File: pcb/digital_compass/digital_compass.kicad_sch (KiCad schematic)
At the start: 0 parts

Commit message: Finish basic digital compass schematic.
* Based on updated xiao-based design
* Also opened in KiCad 7
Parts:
- added BT1: Battery, symbol Device:Battery
- added C1: 0.47uF, symbol Device:C
- added C2: 0.1uF, symbol Device:C
- added R1: 330, symbol Device:R
- added U1: L7805, symbol Regulator_Linear:L7805
- added U2: Seeed Studio XIAO SAMD21, symbol digital_compass:Seeed Studio XIAO SAMD21
- added U3: Level_Shifter, symbol digital_compass:Level_Shifter
- added U4: QMC5883L, symbol digital_compass:QMC5883L
- added U5: Adafruit_Neopixel_Ring_24, symbol digital_compass:Adafruit_Neopixel_Ring_24
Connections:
- new net: C2.1, U1.3 (OUT), U2.14 (5V), U3.10 (HV), U4.1 (VCC), U5.1 (PWR1), U5.2 (PWR2)
- new net: U3.12 (HV1), U4.3 (SCL)
- new net: U3.11 (HV2), U4.4 (SDA)
- new net: U2.6 (PA9_A5_D5_SCL), U3.1 (LV1)
- new net: U2.5 (PA8_A4_D4_SDA), U3.2 (LV2)
- new net: U2.12 (3V3), U3.3 (LV)
- new net: U2.7 (PB08_A6_D6_TX), U3.5 (LV3)
- new net: R1.1, U3.8 (HV3)
- new net: R1.2, U5.3 (Din)
- new net +9V: BT1.1 (+), C1.1, U1.1 (IN)
- new net GND: BT1.2 (-), C1.2, C2.2, U1.2 (GND), U2.13 (GND), U3.4 (GND), U3.9 (GND), U4.2 (GND), U5.5 (GND1), U5.6 (GND2)
- no-connect marks 0 -> 18

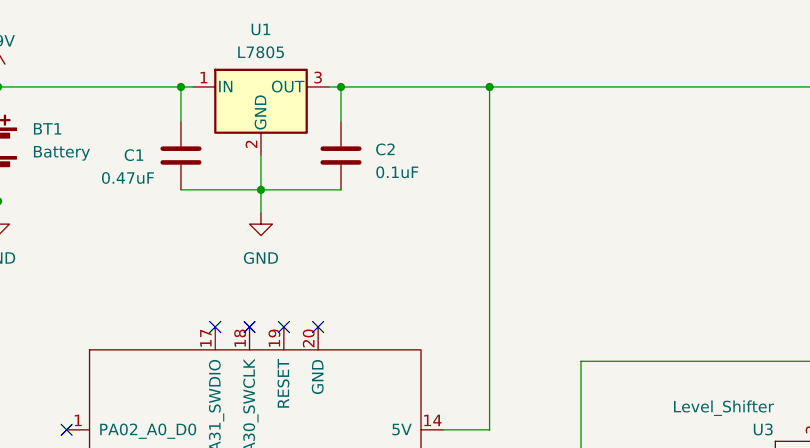
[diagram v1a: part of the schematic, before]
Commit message: Add/update footprints and run fp assignment.
The footprints for the level shifter and magnetometer boards were
created manually, but the xiao symbol/footprint were taken from
https://github.com/Seeed-Studio/OPL_Kicad_Library.

Note that the xiao symbol was lightly tweaked to pass ERC, as the pins
were not properly labeled as power inputs/outputs, bidirectional, etc.
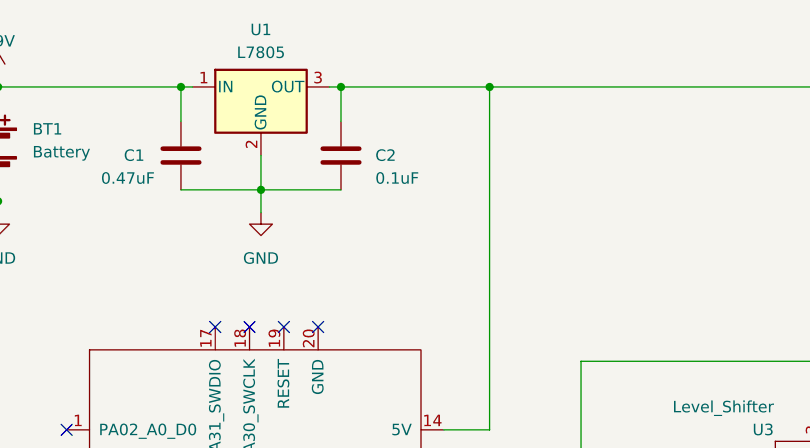
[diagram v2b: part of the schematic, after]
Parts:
- BT1: footprint (none) -> Battery:BatteryHolder_Eagle_12BH611-GR
- C1, C2: footprint (none) -> Capacitor_SMD:C_1206_3216Metric_Pad1.33x1.80mm_HandSolder
- R1: footprint (none) -> Resistor_SMD:R_1206_3216Metric_Pad1.30x1.75mm_HandSolder
- U1: footprint (none) -> Package_TO_SOT_SMD:TO-252-3_TabPin2
- U2: footprint (none) -> digital_compass:XIAO-SAMD21-RP2040-14P-2.54-21X17.8MM (Seeeduino XIAO)
- U3: footprint (none) -> digital_compass:Level_Shifter
- U4: footprint (none) -> digital_compass:QMC5883L
- U5: footprint (none) -> digital_compass:Adafruit Neopixel Ring 24
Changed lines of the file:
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@@
       (effects (font (size 1.27 1.27)) (justify left))
     )
-    (property "Footprint" "" (at 94.9452 63.5 0)
+    (property "Footprint" "Capacitor_SMD:C_1206_3216Metric_Pad1.33x1.80mm_HandSolder" (at 94.9452 63.5 0)
       (effects (font (size 1.27 1.27)) hide)
     )
@@
       (effects (font (size 1.27 1.27)))
     )
-    (property "Footprint" "" (at 103.505 55.88 0)
+    (property "Footprint" "Package_TO_SOT_SMD:TO-252-3_TabPin2" (at 103.505 55.88 0)
       (effects (font (size 1.27 1.27) italic) (justify left) hide)
     )
@@
       (effects (font (size 1.27 1.27)) (justify right))
     )
-    (property "Footprint" "" (at 205.74 97.79 0)
+    (property "Footprint" "digital_compass:QMC5883L" (at 205.74 97.79 0)
       (effects (font (size 1.27 1.27)) hide)
     )
@@
       (effects (font (size 1.27 1.27)) (justify left))
     )
-    (property "Footprint" "" (at 168.91 102.87 0)
+    (property "Footprint" "digital_compass:Level_Shifter" (at 168.91 102.87 0)
       (effects (font (size 1.27 1.27)) hide)
     )
@@
       (effects (font (size 1.27 1.27)) (justify left))
     )
-    (property "Footprint" "" (at 73.66 56.896 90)
+    (property "Footprint" "Battery:BatteryHolder_Eagle_12BH611-GR" (at 73.66 56.896 90)
       (effects (font (size 1.27 1.27)) hide)
     )
@@
       (effects (font (size 1.27 1.27)) (justify left))
     )
-    (property "Footprint" "" (at 187.452 118.11 90)
+    (property "Footprint" "Resistor_SMD:R_1206_3216Metric_Pad1.30x1.75mm_HandSolder" (at 187.452 118.11 90)
       (effects (font (size 1.27 1.27)) hide)
     )
@@
       (effects (font (size 1.27 1.27)) (justify left))
     )
-    (property "Footprint" "" (at 93.98 96.52 0)
+    (property "Footprint" "digital_compass:XIAO-SAMD21-RP2040-14P-2.54-21X17.8MM (Seeeduino XIAO)" (at 93.98 96.52 0)
       (effects (font (size 1.27 1.27)) hide)
     )
@@
   )
   (symbol (lib_id "Device:C") (at 111.76 59.69 0) (unit 1)
-    (in_bom yes) (on_board yes) (dnp no) (fields_autoplaced)
-    (property "Reference" "C2" (at 115.57 59.055 0)
-      (effects (font (size 1.27 1.27)) (justify left))
-    )
-    (property "Value" "0.1uF" (at 115.57 61.595 0)
-      (effects (font (size 1.27 1.27)) (justify left))
-    )
-    (property "Footprint" "" (at 112.7252 63.5 0)
+    (in_bom yes) (on_board yes) (dnp no)
+    (property "Reference" "C2" (at 115.57 59.69 0)
+      (effects (font (size 1.27 1.27)) (justify left))
+    )
+    (property "Value" "0.1uF" (at 115.57 62.23 0)
+      (effects (font (size 1.27 1.27)) (justify left))
+    )
+    (property "Footprint" "Capacitor_SMD:C_1206_3216Metric_Pad1.33x1.80mm_HandSolder" (at 112.7252 63.5 0)
       (effects (font (size 1.27 1.27)) hide)
     )
@@
       (effects (font (size 1.27 1.27)))
     )
-    (property "Footprint" "" (at 241.3 97.79 0)
-      (effects (font (size 1.27 1.27)) hide)
-    )
+    (property "Footprint" "digital_compass:Adafruit Neopixel Ring 24" (at 241.3 97.79 0)
+      (effects (font (size 1.27 1.27)) hide)
+    )

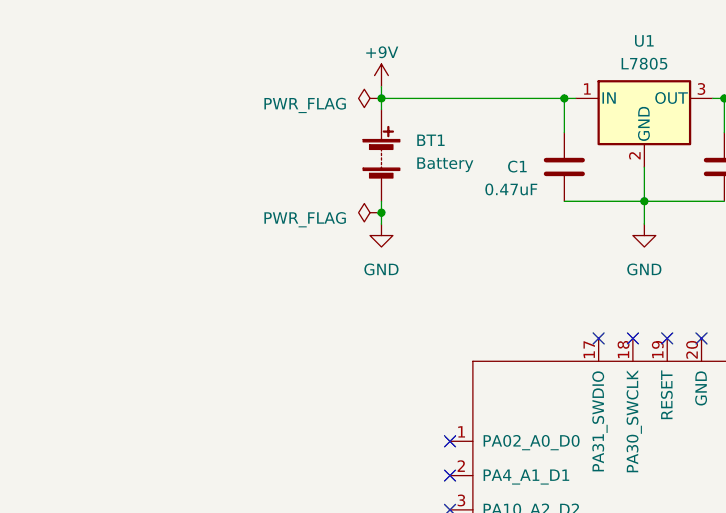
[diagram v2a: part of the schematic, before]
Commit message: Add SPDT slide power switch.
For now we just choose an ok-looking smd footprint but we may need to
make a custom one depending on what we actually find with suppliers.
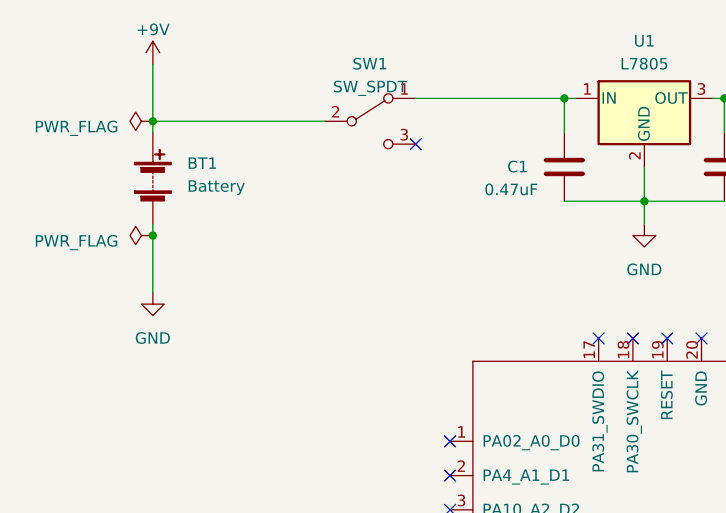
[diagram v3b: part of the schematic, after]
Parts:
- added SW1: SW_SPDT, Button_Switch_SMD:SW_SPDT_PCM12, symbol Switch:SW_SPDT
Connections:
- net +9V: now also SW1.2 (B); no longer C1.1, U1.1 (IN)
- new net: C1.1, SW1.1 (A), U1.1 (IN)
- no-connect marks 18 -> 19
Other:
- moved on the sheet: BT1
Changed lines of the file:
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@@
   (junction (at 128.27 52.07) (diameter 0) (color 0 0 0 0)
   )
-  (junction (at 73.66 64.77) (diameter 0) (color 0 0 0 0)
+  (junction (at 48.26 67.31) (diameter 0) (color 0 0 0 0)
   )
   (junction (at 111.76 52.07) (diameter 0) (color 0 0 0 0)
@@
   (junction (at 93.98 52.07) (diameter 0) (color 0 0 0 0)
   )
-  (junction (at 73.66 52.07) (diameter 0) (color 0 0 0 0)
+  (junction (at 48.26 54.61) (diameter 0) (color 0 0 0 0)
   )
   (junction (at 102.87 63.5) (diameter 0) (color 0 0 0 0)
@@
   (no_connect (at 123.19 113.03))
   (no_connect (at 81.28 93.98))
+  (no_connect (at 77.47 57.15))
   (no_connect (at 81.28 101.6))
   (no_connect (at 217.17 132.08))
@@
     (stroke (width 0) (type default))
   )
-  (wire (pts (xy 73.66 52.07) (xy 73.66 53.34))
+  (wire (pts (xy 48.26 54.61) (xy 48.26 55.88))
     (stroke (width 0) (type default))
   )
@@
     (stroke (width 0) (type default))
   )
+  (wire (pts (xy 77.47 52.07) (xy 93.98 52.07))
+    (stroke (width 0) (type default))
+  )
   (wire (pts (xy 172.72 52.07) (xy 205.74 52.07))
     (stroke (width 0) (type default))
@@
     (stroke (width 0) (type default))
   )
+  (wire (pts (xy 48.26 54.61) (xy 67.31 54.61))
+    (stroke (width 0) (type default))
+  )
   (wire (pts (xy 73.66 113.03) (xy 73.66 137.16))
     (stroke (width 0) (type default))
@@
     (stroke (width 0) (type default))
   )
-  (wire (pts (xy 73.66 52.07) (xy 93.98 52.07))
-    (stroke (width 0) (type default))
-  )
   (wire (pts (xy 81.28 105.41) (xy 76.2 105.41))
     (stroke (width 0) (type default))
@@
     (stroke (width 0) (type default))
   )
-  (wire (pts (xy 73.66 50.8) (xy 73.66 52.07))
+  (wire (pts (xy 48.26 48.26) (xy 48.26 54.61))
     (stroke (width 0) (type default))
   )
@@
     (stroke (width 0) (type default))
   )
-  (wire (pts (xy 73.66 64.77) (xy 73.66 66.04))
+  (wire (pts (xy 48.26 67.31) (xy 48.26 73.66))
     (stroke (width 0) (type default))
   )
@@
     (stroke (width 0) (type default))
   )
-  (wire (pts (xy 73.66 63.5) (xy 73.66 64.77))
+  (wire (pts (xy 48.26 66.04) (xy 48.26 67.31))
     (stroke (width 0) (type default))
   )
@@
     )
   )
-  (symbol (lib_id "power:GND") (at 73.66 66.04 0) (unit 1)
-    (in_bom yes) (on_board yes) (dnp no) (fields_autoplaced)
-    (property "Reference" "#PWR02" (at 73.66 72.39 0)
-      (effects (font (size 1.27 1.27)) hide)
-    )
-    (property "Value" "GND" (at 73.66 71.12 0)
-      (effects (font (size 1.27 1.27)))
-    )
-    (property "Footprint" "" (at 73.66 66.04 0)
-      (effects (font (size 1.27 1.27)) hide)
-    )
-    (property "Datasheet" "" (at 73.66 66.04 0)
+  (symbol (lib_id "power:GND") (at 48.26 73.66 0) (unit 1)
+    (in_bom yes) (on_board yes) (dnp no) (fields_autoplaced)
+    (property "Reference" "#PWR02" (at 48.26 80.01 0)
+      (effects (font (size 1.27 1.27)) hide)
+    )
+    (property "Value" "GND" (at 48.26 78.74 0)
+      (effects (font (size 1.27 1.27)))
+    )
+    (property "Footprint" "" (at 48.26 73.66 0)
+      (effects (font (size 1.27 1.27)) hide)
+    )
+    (property "Datasheet" "" (at 48.26 73.66 0)
       (effects (font (size 1.27 1.27)) hide)
     )
@@
     )
   )
-  (symbol (lib_id "power:PWR_FLAG") (at 73.66 52.07 90) (unit 1)
+  (symbol (lib_id "power:PWR_FLAG") (at 48.26 54.61 90) (unit 1)
     (in_bom yes) (on_board yes) (dnp no)
-    (property "Reference" "#FLG01" (at 71.755 52.07 0)
-      (effects (font (size 1.27 1.27)) hide)
-    )
-    (property "Value" "PWR_FLAG" (at 69.85 52.705 90)
-      (effects (font (size 1.27 1.27)) (justify left))
-    )
-    (property "Footprint" "" (at 73.66 52.07 0)
-      (effects (font (size 1.27 1.27)) hide)
-    )
-    (property "Datasheet" "~" (at 73.66 52.07 0)
+    (property "Reference" "#FLG01" (at 46.355 54.61 0)
+      (effects (font (size 1.27 1.27)) hide)
+    )
+    (property "Value" "PWR_FLAG" (at 44.45 55.245 90)
+      (effects (font (size 1.27 1.27)) (justify left))
+    )
+    (property "Footprint" "" (at 48.26 54.61 0)
+      (effects (font (size 1.27 1.27)) hide)
+    )
+    (property "Datasheet" "~" (at 48.26 54.61 0)
       (effects (font (size 1.27 1.27)) hide)
     )
@@
     )
   )
-  (symbol (lib_id "Device:Battery") (at 73.66 58.42 0) (unit 1)
+  (symbol (lib_id "Device:Battery") (at 48.26 60.96 0) (unit 1)
     (in_bom yes) (on_board yes) (dnp no)
-    (property "Reference" "BT1" (at 77.47 56.7689 0)
-      (effects (font (size 1.27 1.27)) (justify left))
-    )
-    (property "Value" "Battery" (at 77.47 59.3089 0)
-      (effects (font (size 1.27 1.27)) (justify left))
-    )
-    (property "Footprint" "Battery:BatteryHolder_Eagle_12BH611-GR" (at 73.66 56.896 90)
-      (effects (font (size 1.27 1.27)) hide)
-    )
-    (property "Datasheet" "~" (at 73.66 56.896 90)
+    (property "Reference" "BT1" (at 52.07 59.3089 0)
+      (effects (font (size 1.27 1.27)) (justify left))
+    )
+    (property "Value" "Battery" (at 52.07 61.8489 0)
+      (effects (font (size 1.27 1.27)) (justify left))
+    )
+    (property "Footprint" "Battery:BatteryHolder_Eagle_12BH611-GR" (at 48.26 59.436 90)
+      (effects (font (size 1.27 1.27)) hide)
+    )
+    (property "Datasheet" "~" (at 48.26 59.436 90)
       (effects (font (size 1.27 1.27)) hide)
     )
@@
     )
   )
-  (symbol (lib_id "power:+9V") (at 73.66 50.8 0) (unit 1)
-    (in_bom yes) (on_board yes) (dnp no) (fields_autoplaced)
-    (property "Reference" "#PWR01" (at 73.66 54.61 0)
-      (effects (font (size 1.27 1.27)) hide)
-    )
-    (property "Value" "+9V" (at 73.66 46.99 0)
-      (effects (font (size 1.27 1.27)))
-    )
-    (property "Footprint" "" (at 73.66 50.8 0)
-      (effects (font (size 1.27 1.27)) hide)
-    )
-    (property "Datasheet" "" (at 73.66 50.8 0)
+  (symbol (lib_id "power:+9V") (at 48.26 48.26 0) (unit 1)
+    (in_bom yes) (on_board yes) (dnp no) (fields_autoplaced)
+    (property "Reference" "#PWR01" (at 48.26 52.07 0)
+      (effects (font (size 1.27 1.27)) hide)
+    )
+    (property "Value" "+9V" (at 48.26 44.45 0)
+      (effects (font (size 1.27 1.27)))
+    )
+    (property "Footprint" "" (at 48.26 48.26 0)
+      (effects (font (size 1.27 1.27)) hide)
+    )
+    (property "Datasheet" "" (at 48.26 48.26 0)
       (effects (font (size 1.27 1.27)) hide)
     )
@@
     )
   )
+  (symbol (lib_id "Switch:SW_SPDT") (at 72.39 54.61 0) (unit 1)
+    (in_bom yes) (on_board yes) (dnp no) (fields_autoplaced)
+    (property "Reference" "SW1" (at 72.39 48.26 0)
+      (effects (font (size 1.27 1.27)))
+    )
+    (property "Value" "SW_SPDT" (at 72.39 50.8 0)
+      (effects (font (size 1.27 1.27)))
+    )
+    (property "Footprint" "Button_Switch_SMD:SW_SPDT_PCM12" (at 72.39 54.61 0)
+      (effects (font (size 1.27 1.27)) hide)
+    )
+    (property "Datasheet" "~" (at 72.39 54.61 0)
+      (effects (font (size 1.27 1.27)) hide)
+    )
+    (pin "1")
+    (pin "2")
+    (pin "3")
+    (instances
+      (project "digital_compass"
+        (path "/baf13a8d-d2e9-47e7-8ed6-5dc9a1813536"
+          (reference "SW1") (unit 1)
+        )
+      )
+    )
+  )
   (symbol (lib_id "Device:C") (at 111.76 59.69 0) (unit 1)
     (in_bom yes) (on_board yes) (dnp no)
@@
     )
   )
-  (symbol (lib_id "power:PWR_FLAG") (at 73.66 64.77 90) (unit 1)
-    (in_bom yes) (on_board yes) (dnp no) (fields_autoplaced)
-    (property "Reference" "#FLG02" (at 71.755 64.77 0)
-      (effects (font (size 1.27 1.27)) hide)
-    )
-    (property "Value" "PWR_FLAG" (at 69.85 65.405 90)
-      (effects (font (size 1.27 1.27)) (justify left))
-    )
-    (property "Footprint" "" (at 73.66 64.77 0)
-      (effects (font (size 1.27 1.27)) hide)
-    )
-    (property "Datasheet" "~" (at 73.66 64.77 0)
-      (effects (font (size 1.27 1.27)) hide)
-    )
+  (symbol (lib_id "power:PWR_FLAG") (at 48.26 67.31 90) (unit 1)
+    (in_bom yes) (on_board yes) (dnp no) (fields_autoplaced)
+    (property "Reference" "#FLG02" (at 46.355 67.31 0)
+      (effects (font (size 1.27 1.27)) hide)
+    )
+    (property "Value" "PWR_FLAG" (at 44.45 67.945 90)
+      (effects (font (size 1.27 1.27)) (justify left))
+    )
+    (property "Footprint" "" (at 48.26 67.31 0)
+      (effects (font (size 1.27 1.27)) hide)
+    )
+    (property "Datasheet" "~" (at 48.26 67.31 0)
+      (effects (font (size 1.27 1.27)) hide)
+    )

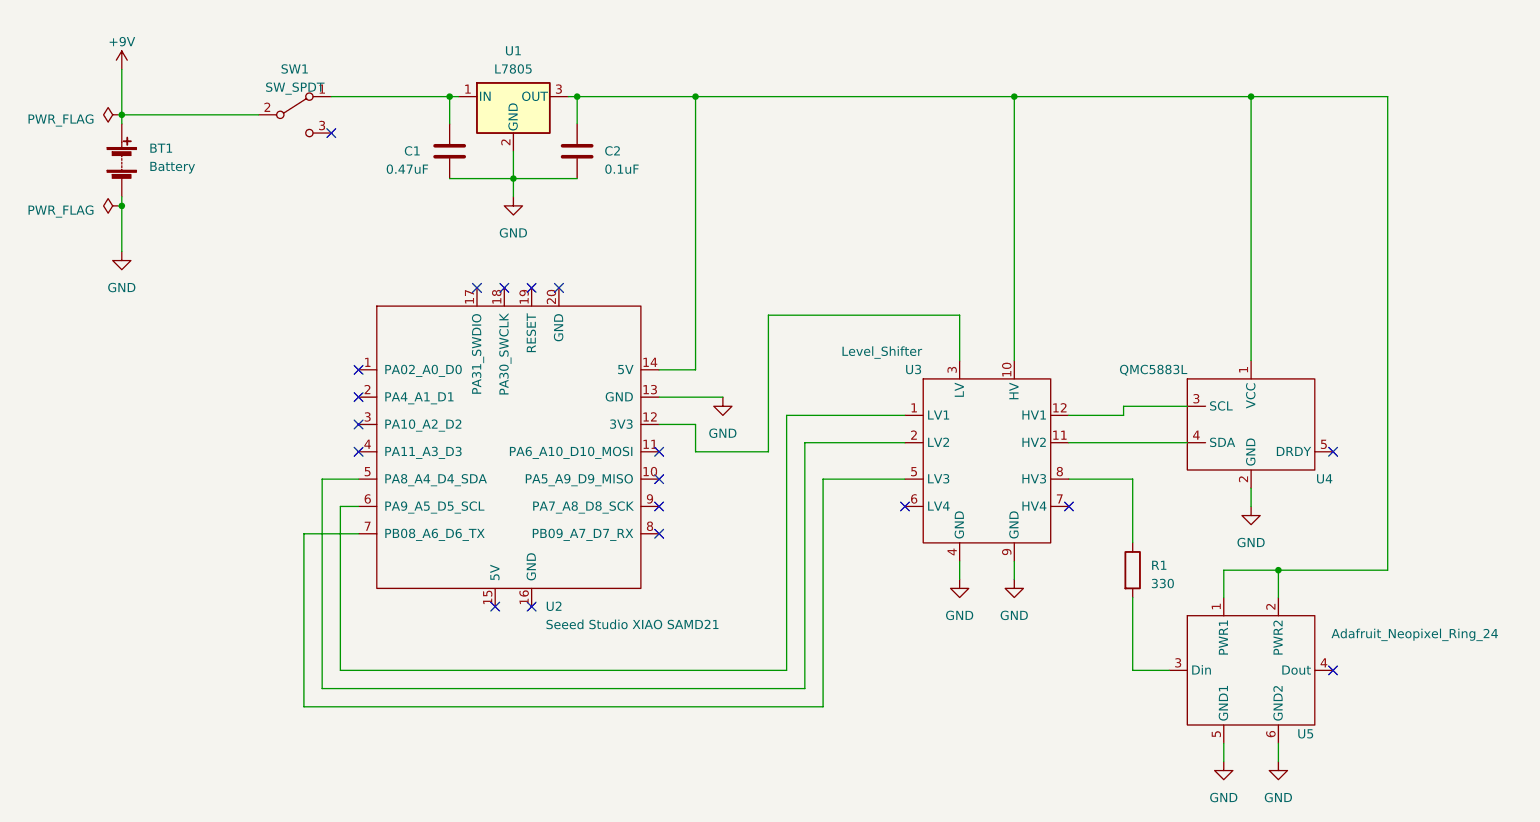
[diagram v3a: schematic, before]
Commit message: Use custom footprint for SPDT switch.
Based on https://www.ckswitches.com/media/1422/js.pdf. Also move the
switch to the regulated side of the L7805, as this switch can only
handle up to 6V.
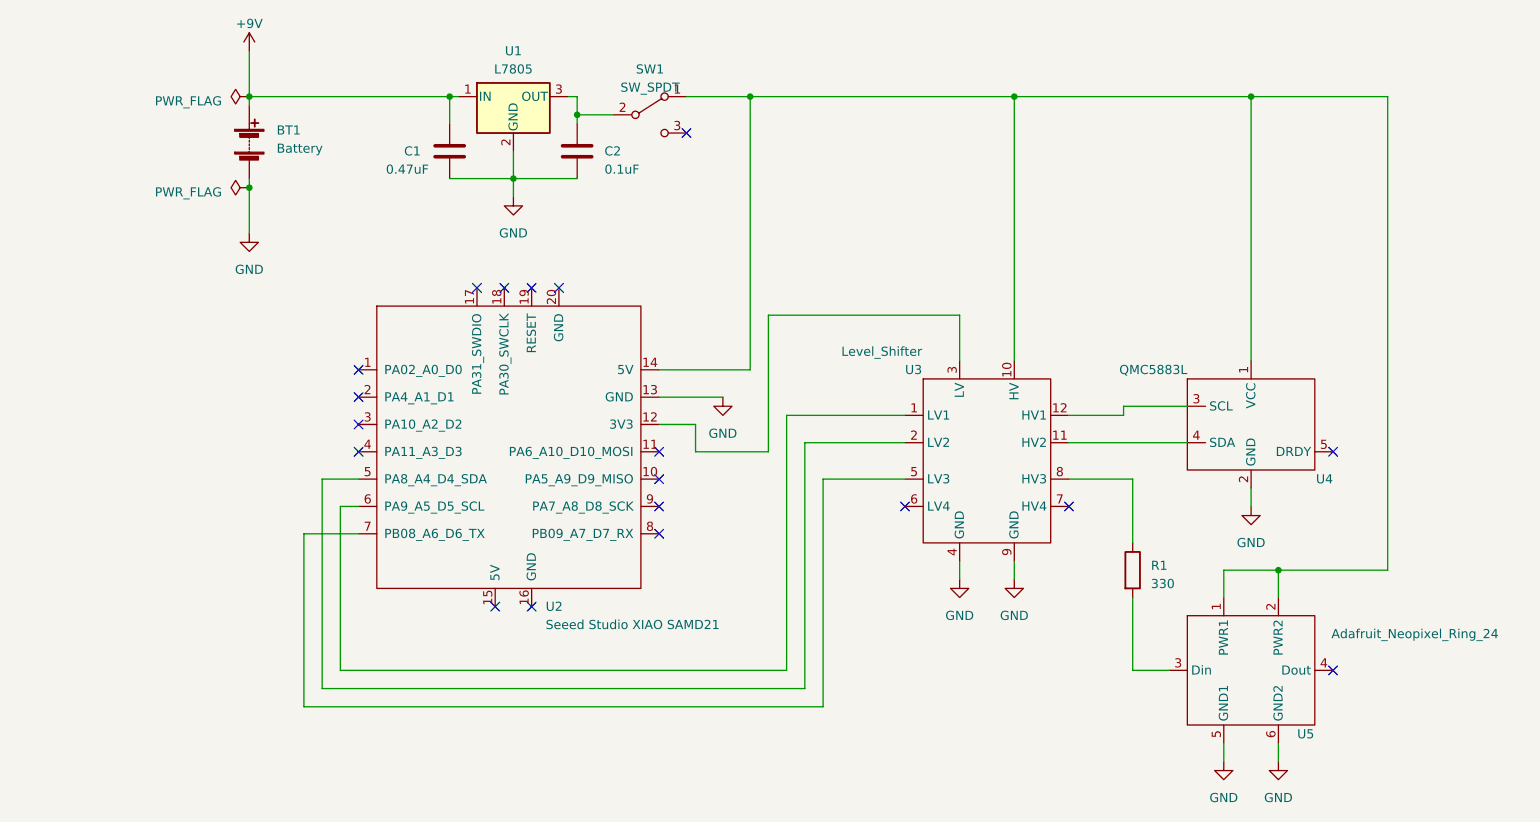
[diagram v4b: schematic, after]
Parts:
- SW1: footprint Button_Switch_SMD:SW_SPDT_PCM12 -> digital_compass:JS102011SCQN_SPDT_Switch
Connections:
- net +9V: now also C1.1, U1.1 (IN); no longer SW1.2 (B)
- net at U2.14 (5V), U3.10 (HV), U4.1 (VCC)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: now also SW1.1 (A); no longer C2.1, U1.3 (OUT)
- new net: C2.1, SW1.2 (B), U1.3 (OUT)
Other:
- moved on the sheet: BT1, SW1
